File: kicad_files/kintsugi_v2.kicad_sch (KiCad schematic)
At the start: 75 parts

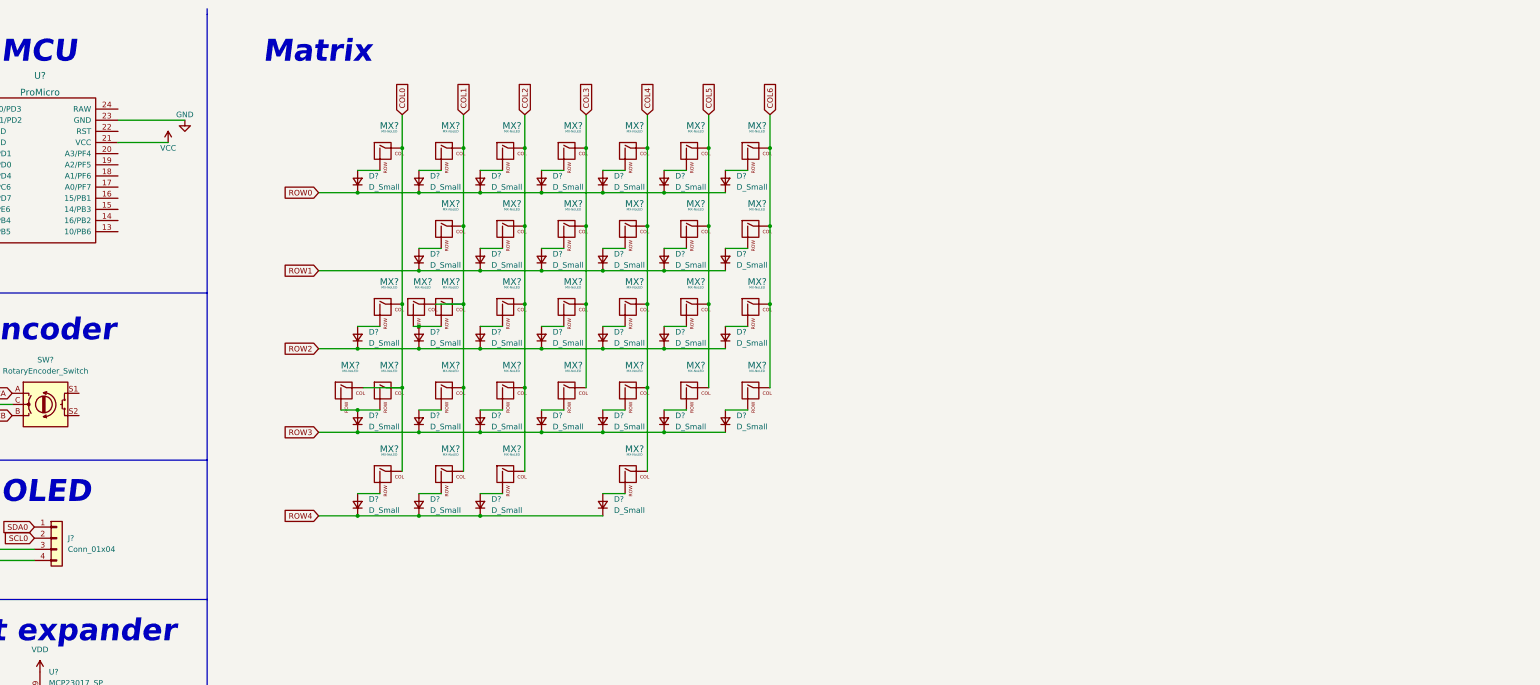
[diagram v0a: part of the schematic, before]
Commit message: Added tentative switch matrix.
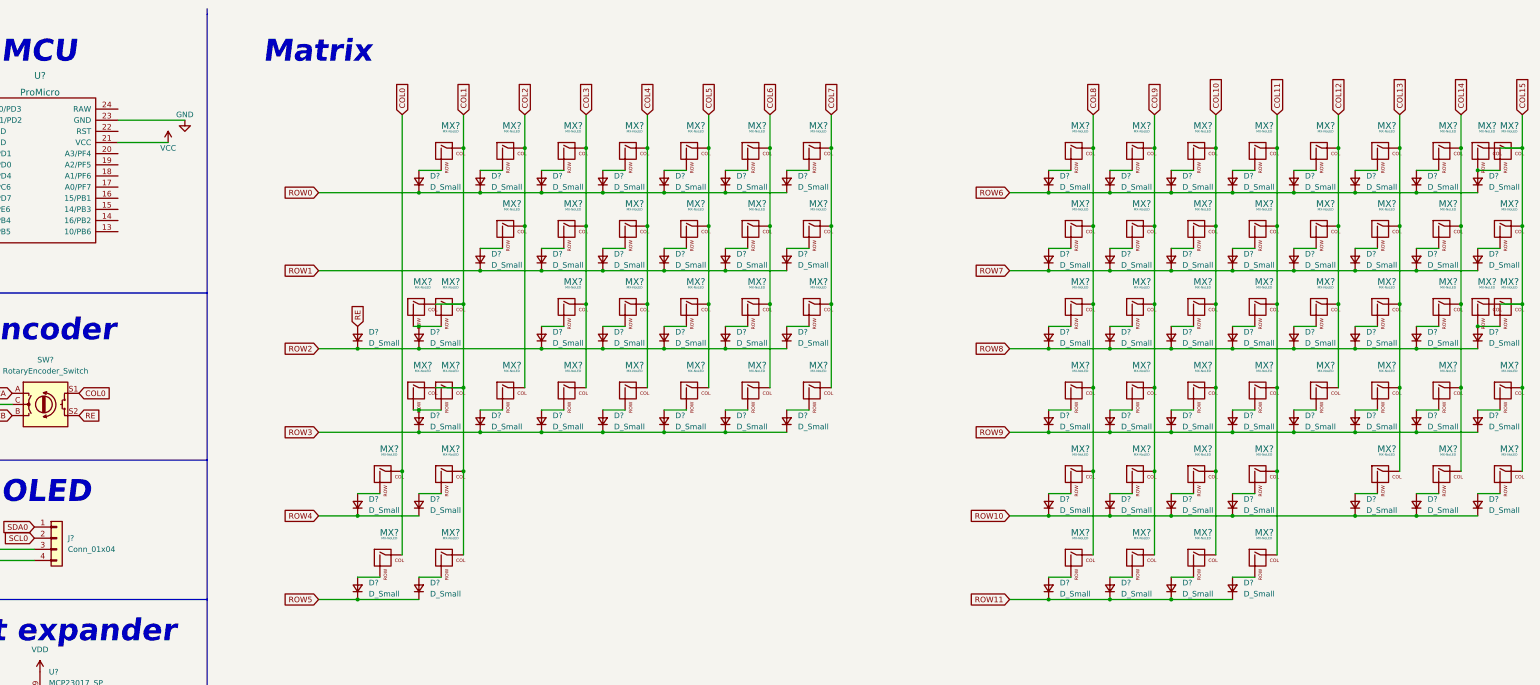
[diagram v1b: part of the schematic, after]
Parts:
- removed D? (x4): D_Small, symbol Device:D_Small
- removed MX? (x4): MX-NoLED, symbol MX_Alps_Hybrid:MX-NoLED
- added D? (x47): D_Small, symbol Device:D_Small
- added MX? (x48): MX-NoLED, symbol MX_Alps_Hybrid:MX-NoLED
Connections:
- net COL0: now also SW?.S1, MX?.1 (COL), MX?.1 (COL); no longer MX?.1 (COL), MX?.1 (COL), MX?.1 (COL)
- net COL1: now also MX?.1 (COL), MX?.1 (COL), MX?.1 (COL), MX?.1 (COL); no longer MX?.1 (COL), MX?.1 (COL), MX?.1 (COL)
- net COL2: now also MX?.1 (COL), MX?.1 (COL), MX?.1 (COL); no longer MX?.1 (COL), MX?.1 (COL), MX?.1 (COL), MX?.1 (COL)
- net COL3: now also MX?.1 (COL), MX?.1 (COL), MX?.1 (COL), MX?.1 (COL); no longer MX?.1 (COL), MX?.1 (COL), MX?.1 (COL), MX?.1 (COL)
- net COL4: now also MX?.1 (COL), MX?.1 (COL), MX?.1 (COL), MX?.1 (COL); no longer MX?.1 (COL), MX?.1 (COL), MX?.1 (COL), MX?.1 (COL)
- net COL5: now also MX?.1 (COL), MX?.1 (COL), MX?.1 (COL), MX?.1 (COL); no longer MX?.1 (COL), MX?.1 (COL), MX?.1 (COL), MX?.1 (COL)
- net COL6: now also MX?.1 (COL), MX?.1 (COL), MX?.1 (COL), MX?.1 (COL); no longer MX?.1 (COL), MX?.1 (COL), MX?.1 (COL), MX?.1 (COL)
- net ROW2: now also D?.1 (K)
- net ROW4: now also D?.1 (K)
- net RE: now reaches SW?.S2
- net RE: now also D?.2 (A)
- new net: D?.2 (A), MX?.2 (ROW) (x44)
- new net: D?.2 (A), MX?.2 (ROW), MX?.2 (ROW) (x2)
- new net COL10: MX?.1 (COL), MX?.1 (COL), MX?.1 (COL), MX?.1 (COL), MX?.1 (COL), MX?.1 (COL)
- new net COL11: MX?.1 (COL), MX?.1 (COL), MX?.1 (COL), MX?.1 (COL), MX?.1 (COL), MX?.1 (COL)
- new net COL12: MX?.1 (COL), MX?.1 (COL), MX?.1 (COL), MX?.1 (COL)
- new net COL13: MX?.1 (COL), MX?.1 (COL), MX?.1 (COL), MX?.1 (COL), MX?.1 (COL)
- new net COL14: MX?.1 (COL), MX?.1 (COL), MX?.1 (COL), MX?.1 (COL), MX?.1 (COL)
- new net COL15: MX?.1 (COL), MX?.1 (COL), MX?.1 (COL), MX?.1 (COL), MX?.1 (COL), MX?.1 (COL), MX?.1 (COL)
- new net COL7: MX?.1 (COL), MX?.1 (COL), MX?.1 (COL), MX?.1 (COL)
- new net COL8: MX?.1 (COL), MX?.1 (COL), MX?.1 (COL), MX?.1 (COL), MX?.1 (COL), MX?.1 (COL)
- new net COL9: MX?.1 (COL), MX?.1 (COL), MX?.1 (COL), MX?.1 (COL), MX?.1 (COL), MX?.1 (COL)
- new net ROW10: D?.1 (K), D?.1 (K), D?.1 (K), D?.1 (K), D?.1 (K), D?.1 (K), D?.1 (K)
- new net ROW11: D?.1 (K), D?.1 (K), D?.1 (K), D?.1 (K)
- new net ROW5: D?.1 (K), D?.1 (K)
- new net ROW6: D?.1 (K), D?.1 (K), D?.1 (K), D?.1 (K), D?.1 (K), D?.1 (K), D?.1 (K), D?.1 (K)
- new net ROW7: D?.1 (K), D?.1 (K), D?.1 (K), D?.1 (K), D?.1 (K), D?.1 (K), D?.1 (K), D?.1 (K)
- new net ROW8: D?.1 (K), D?.1 (K), D?.1 (K), D?.1 (K), D?.1 (K), D?.1 (K), D?.1 (K), D?.1 (K)
- new net ROW9: D?.1 (K), D?.1 (K), D?.1 (K), D?.1 (K), D?.1 (K), D?.1 (K), D?.1 (K), D?.1 (K)
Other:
- moved on the sheet: D?, MX?

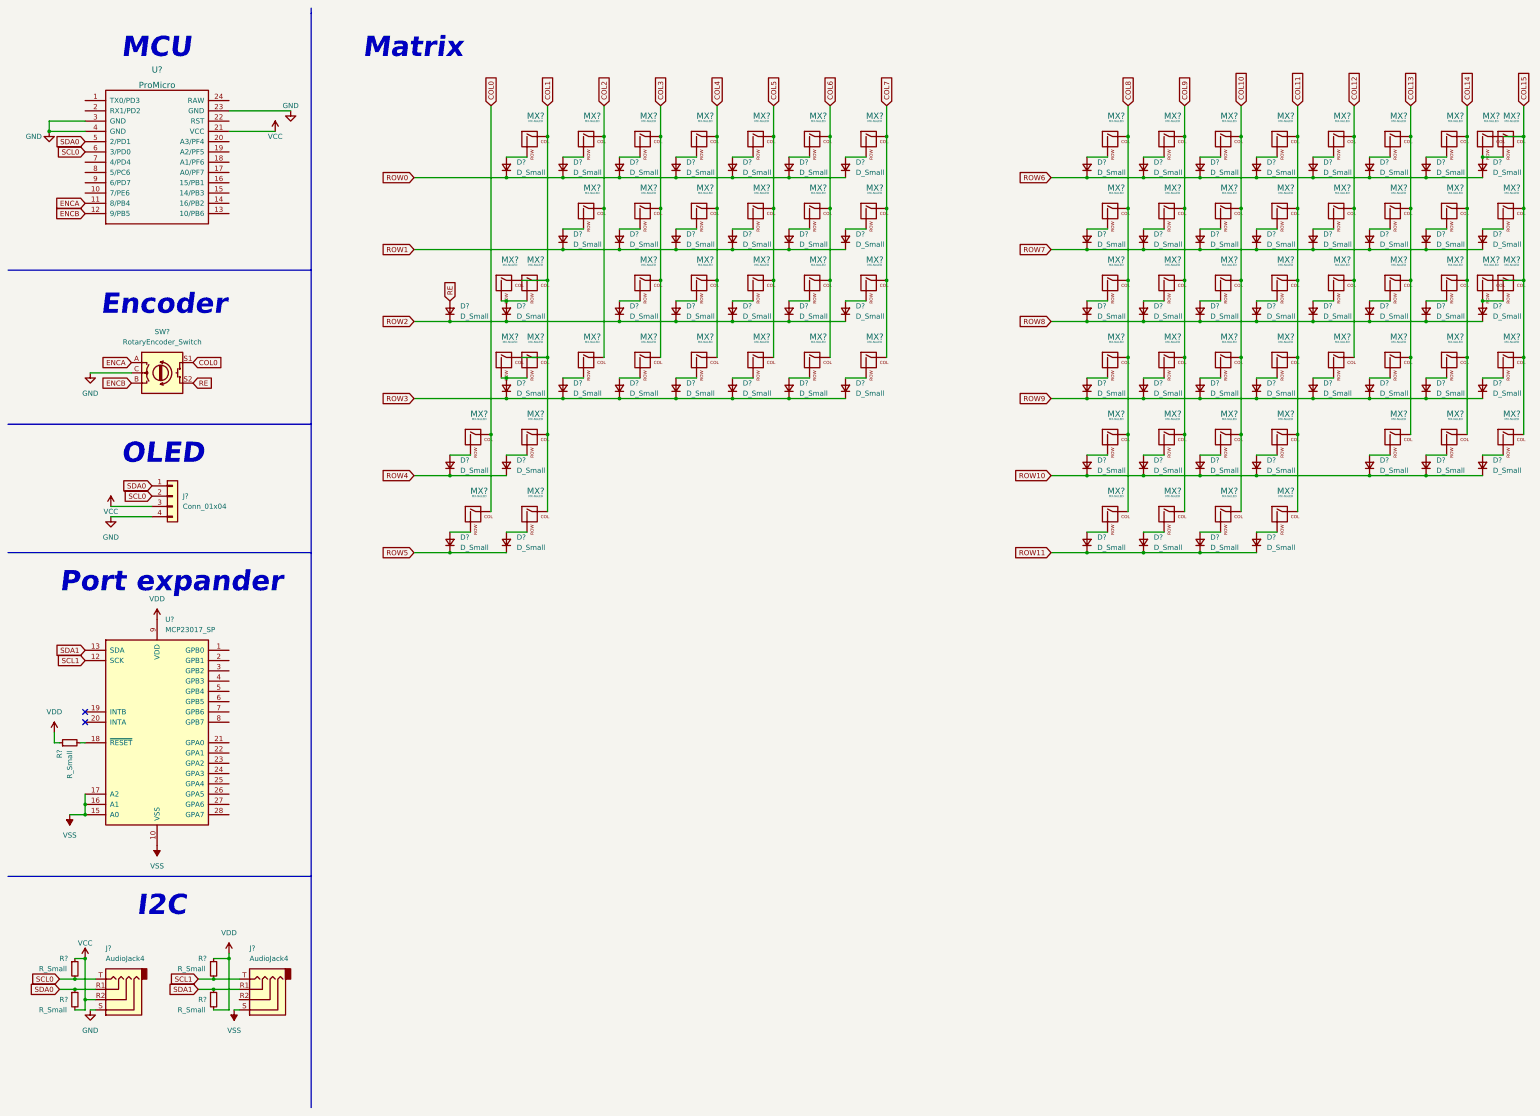
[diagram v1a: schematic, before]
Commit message: Completed schematic and linked footprints.
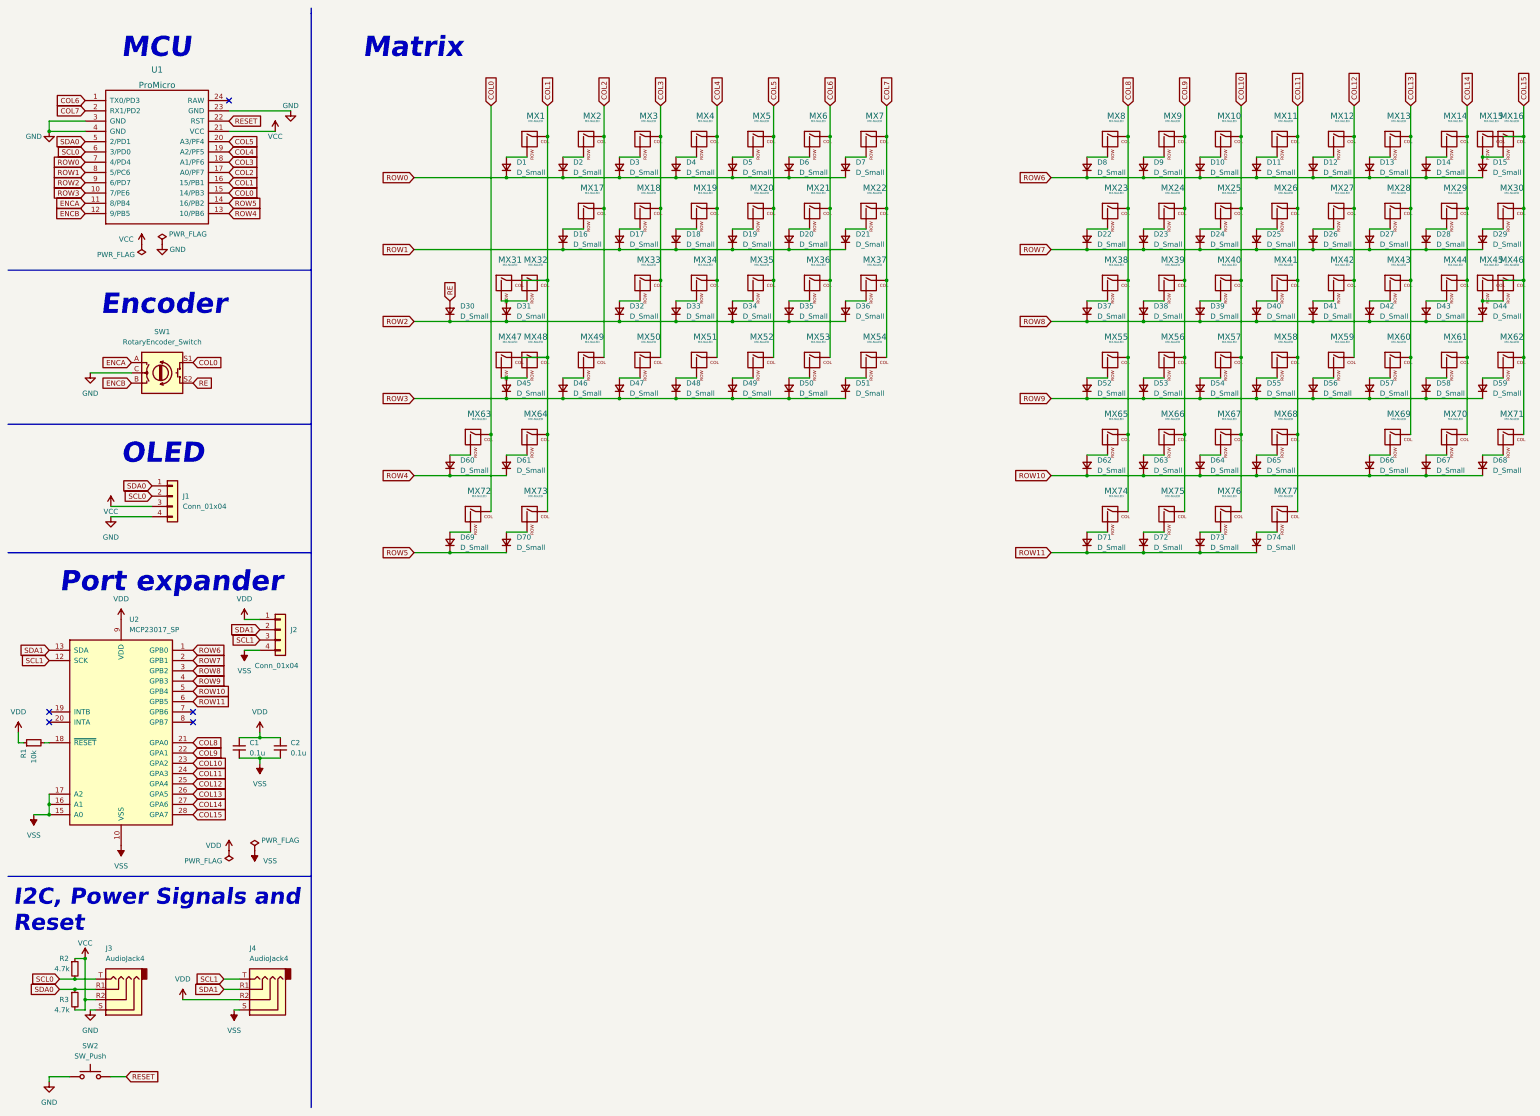
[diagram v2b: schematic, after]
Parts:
- removed R? (x2): R_Small, symbol Device:R_Small
- added C1, C2: 0.1u, Capacitor_SMD:C_0805_2012Metric_Pad1.18x1.45mm_HandSolder, symbol Device:C_Small
- added J2: Conn_01x04, Connector_PinHeader_2.54mm:PinHeader_1x04_P2.54mm_Vertical, symbol Connector_Generic:Conn_01x04
- added SW2: SW_Push, Button_Switch_SMD:SW_SPST_SKQG_WithStem, symbol Switch:SW_Push
- D1, D10, D11, D12, D13, D14, D15, D16, D17, D18, D19, D2, D20, D21, D22, D23, D24, D25, D26, D27, D28, D29, D3, D30, D31, D32, D33, D34, D35, D36, D37, D38, D39, D4, D40, D41, D42, D43, D44, D45, D46, D47, D48, D49, D5, D50, D51, D52, D53, D54, D55, D56, D57, D58, D59, D6, D60, D61, D62, D63, D64, D65, D66, D67, D68, D69, D7, D70, D71, D72, D73, D74, D8, D9: renamed from D?; footprint (none) -> Keebio-Parts:D_SOD123
- J1: renamed from J?; footprint (none) -> Connector_PinHeader_2.54mm:PinHeader_1x04_P2.54mm_Vertical
- J3, J4: renamed from J?; footprint (none) -> Keebio-Parts:TRRS-PJ-320A
- MX1, MX10, MX11, MX12, MX13, MX14, MX15, MX16, MX17, MX18, MX19, MX2, MX20, MX21, MX22, MX23, MX24, MX25, MX26, MX27, MX28, MX29, MX3, MX30, MX31, MX32, MX33, MX34, MX35, MX36, MX37, MX38, MX39, MX4, MX40, MX41, MX42, MX43, MX44, MX45, MX46, MX47, MX48, MX49, MX5, MX50, MX51, MX52, MX53, MX54, MX55, MX56, MX57, MX58, MX59, MX6, MX60, MX61, MX62, MX63, MX64, MX65, MX66, MX67, MX68, MX69, MX7, MX70, MX71, MX72, MX73, MX74, MX75, MX76, MX77, MX8, MX9: renamed from MX?; footprint (none) -> acheron_MXH_metalrings:MX100H
- R1: renamed from R?; value R_Small -> 10k; footprint (none) -> Resistor_SMD:R_0805_2012Metric_Pad1.20x1.40mm_HandSolder
- R2, R3: renamed from R?; value R_Small -> 4.7k; footprint (none) -> Resistor_SMD:R_0805_2012Metric_Pad1.20x1.40mm_HandSolder
- SW1: renamed from SW?; footprint (none) -> Rotary_Encoder:RotaryEncoder_Alps_EC11E-Switch_Vertical_H20mm
- U1: renamed from U?; footprint (none) -> Keebio-Parts:ArduinoProMicro
- gave numbers to parts that had none: 1
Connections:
- net COL0: now also U1.15 (14/PB3)
- net COL1: now also U1.16 (15/PB1)
- net COL10: now also U2.23 (GPA2)
- net COL11: now also U2.24 (GPA3)
- net COL12: now also U2.25 (GPA4)
- net COL13: now also U2.26 (GPA5)
- net COL14: now also U2.27 (GPA6)
- net COL15: now also U2.28 (GPA7)
- net COL2: now also U1.17 (A0/PF7)
- net COL3: now also U1.18 (A1/PF6)
- net COL4: now also U1.19 (A2/PF5)
- net COL5: now also U1.20 (A3/PF4)
- net COL6: now also U1.1 (TX0/PD3)
- net COL7: now also U1.2 (RX1/PD2)
- net COL8: now also U2.21 (GPA0)
- net COL9: now also U2.22 (GPA1)
- net GND: now also SW2.1
- net ROW0: now also U1.7 (4/PD4)
- net ROW1: now also U1.8 (5/PC6)
- net ROW10: now also U2.5 (GPB4)
- net ROW11: now also U2.6 (GPB5)
- net ROW2: now also U1.9 (6/PD7)
- net ROW3: now also U1.10 (7/PE6)
- net ROW4: now also U1.13 (10/PB6)
- net ROW5: now also U1.14 (16/PB2)
- net ROW6: now also U2.1 (GPB0)
- net ROW7: now also U2.2 (GPB1)
- net ROW8: now also U2.3 (GPB2)
- net ROW9: now also U2.4 (GPB3)
- net SCL1: now also J2.3 (Pin_3)
- net SDA1: now also J2.2 (Pin_2)
- net VDD: now also J4.R2, C1.1, C2.1, J2.1 (Pin_1)
- net VSS: now also C1.2, C2.2, J2.4 (Pin_4)
- net RESET: now reaches U1.22 (RST)
- net RESET: now also SW2.2
- no-connect marks 2 -> 5
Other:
- note added: "I2C, Power Signals and Reset"
- note removed: "I2C"
- moved on the sheet: R1, U2

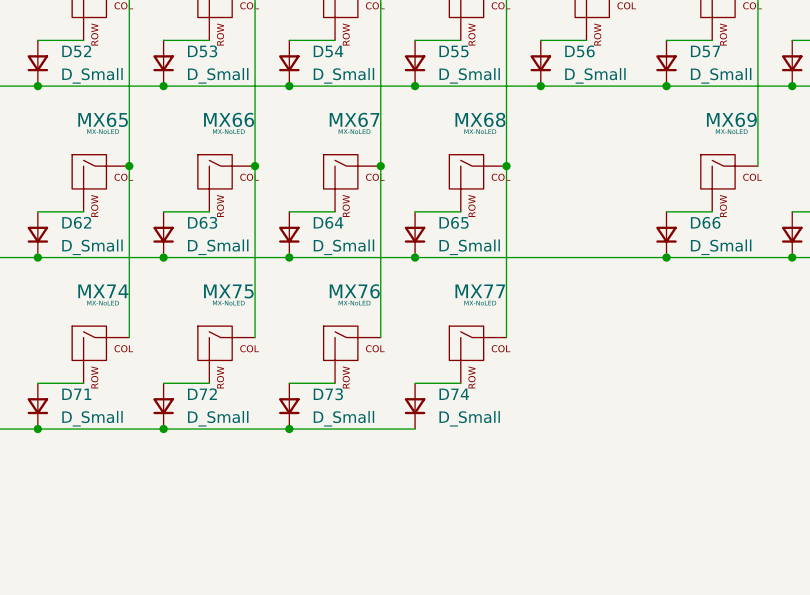
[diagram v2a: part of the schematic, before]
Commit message: Added preliminary arrangement of the components on the PCB file.
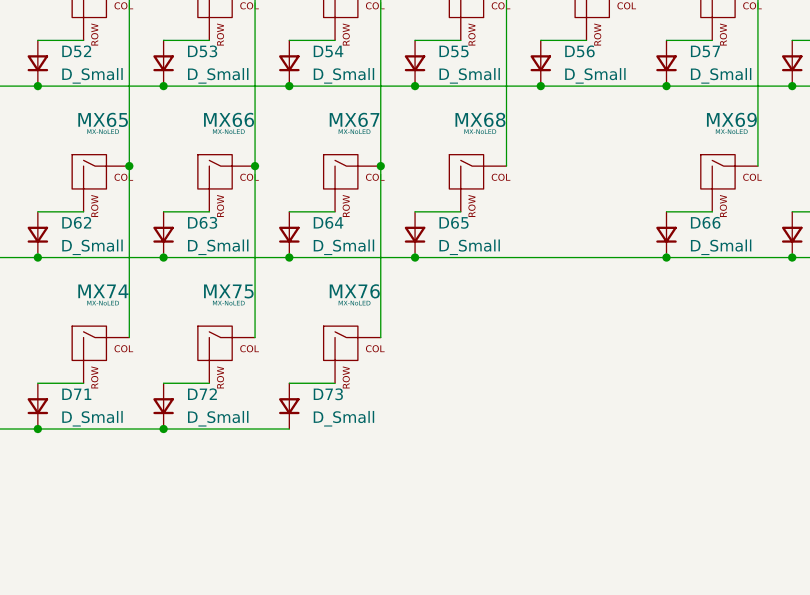
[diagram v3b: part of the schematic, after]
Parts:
- removed D74: D_Small, Keebio-Parts:D_SOD123, symbol Device:D_Small
- removed MX77: MX-NoLED, acheron_MXH_metalrings:MX100H, symbol MX_Alps_Hybrid:MX-NoLED
- D1, D10, D11, D12, D13, D14, D15, D16, D17, D18, D19, D2, D20, D21, D22, D23, D24, D25, D26, D27, D28, D29, D3, D30, D31, D32, D33, D34, D35, D36, D37, D38, D39, D4, D40, D41, D42, D43, D44, D45, D46, D47, D48, D49, D5, D50, D51, D52, D53, D54, D55, D56, D57, D58, D59, D6, D60, D61, D62, D63, D64, D65, D66, D67, D68, D69, D7, D70, D71, D72, D73, D8, D9: footprint Keebio-Parts:D_SOD123 -> custom_parts:D_SOD-123_silkscreen
- J3, J4: footprint Keebio-Parts:TRRS-PJ-320A -> custom_parts:TRRS-PJ-320A
- MX16: footprint acheron_MXH_metalrings:MX100H -> acheron_MXH_metalrings:MX200H
- MX17, MX30: footprint acheron_MXH_metalrings:MX100H -> acheron_MXH_metalrings:MX150H
- MX31, MX47, MX63, MX64, MX66, MX67, MX68, MX72: footprint acheron_MXH_metalrings:MX100H -> acheron_MXH_metalrings:MX125H
- MX32, MX60: footprint acheron_MXH_metalrings:MX100H -> acheron_MXH_metalrings:MX175H
- MX45, MX48: footprint acheron_MXH_metalrings:MX100H -> acheron_MXH_metalrings:MX225H
- MX46: footprint acheron_MXH_metalrings:MX100H -> acheron_MXH_metalrings:MX_ISOEnterH
- MX65: footprint acheron_MXH_metalrings:MX100H -> acheron_MXH_metalrings:MX225HR
- MX73: footprint acheron_MXH_metalrings:MX100H -> acheron_MXH_metalrings:MX275HR
